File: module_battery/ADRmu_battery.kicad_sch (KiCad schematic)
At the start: 81 parts, among them J101 Harting 09042326831, Q101 Q_NMOS_GDS, Q102 Q_NMOS_GDS, U101 BQ7791500, U102 LTC4079, U103 L7812

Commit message: Update ADRmu_battery.kicad_sch
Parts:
- removed NT101: NetTie_2, NetTie:NetTie-2_SMD_Pad2.0mm, symbol Device:NetTie_2
- added F?: 2A, Fuse:Fuse_1812_4532Metric, symbol Device:Polyfuse
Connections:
- net -BATT: now also F?.1; no longer R107.1, R108.1
- net GND: now also R107.1, R108.1, F?.2

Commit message: asdf
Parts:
- gave numbers to parts that had none: 26
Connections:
- net -BATT: no longer R106.1
- net GND: now also R106.1
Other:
- moved on the sheet: C105

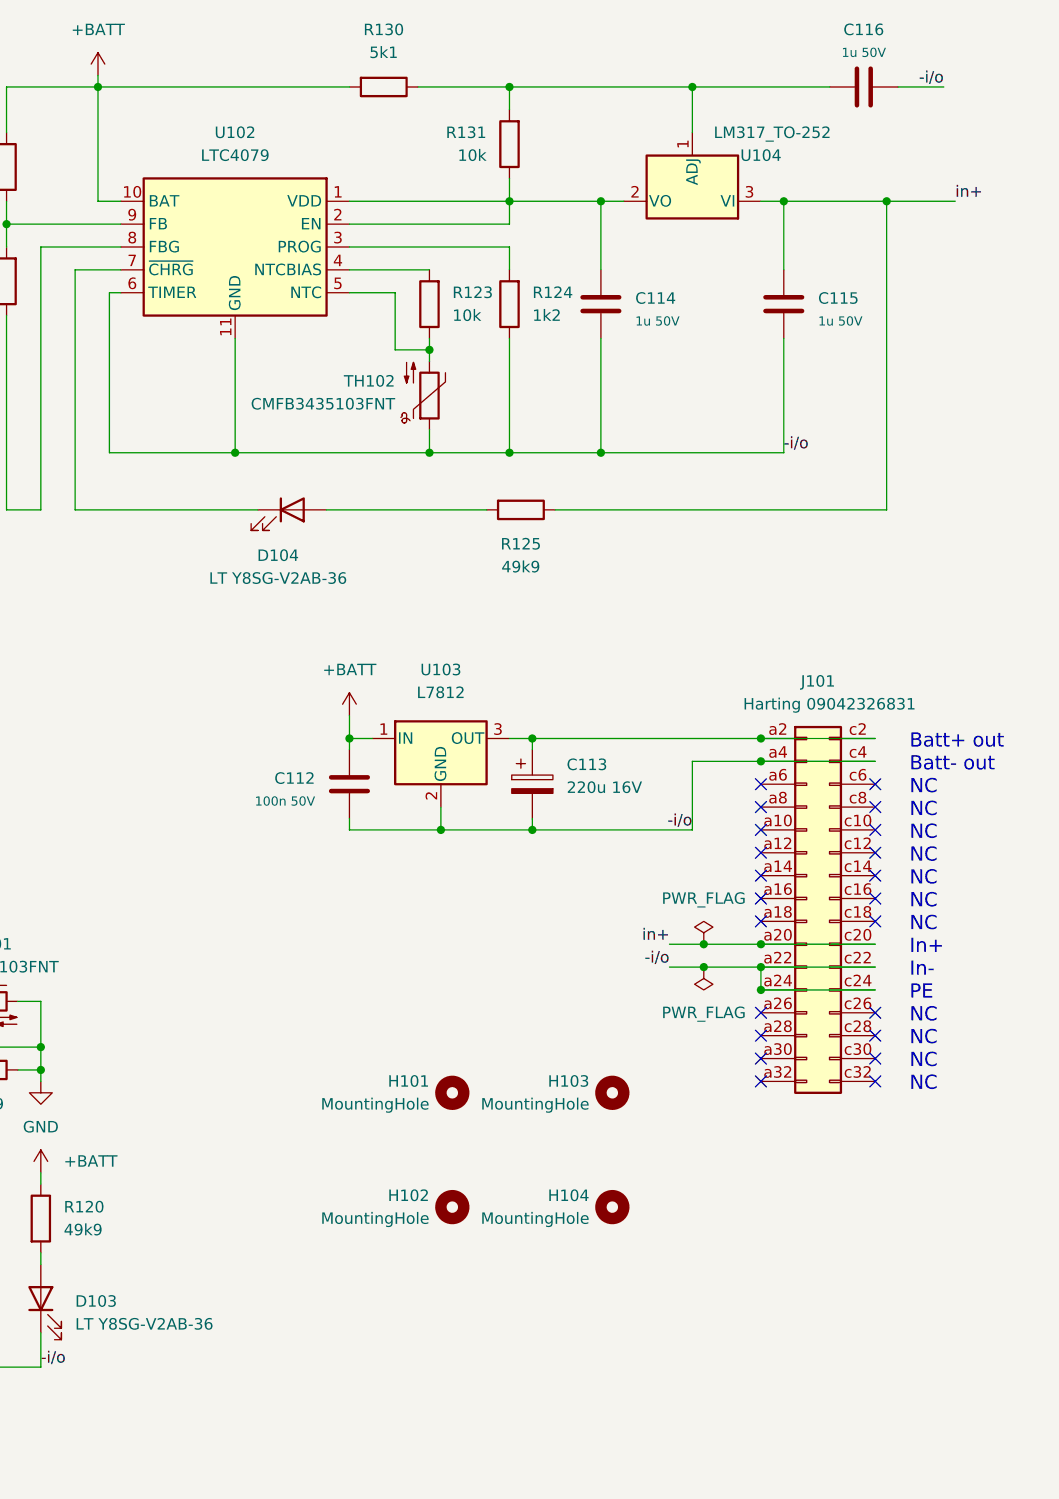
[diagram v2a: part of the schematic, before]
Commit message: battery module rev 0.3 routed
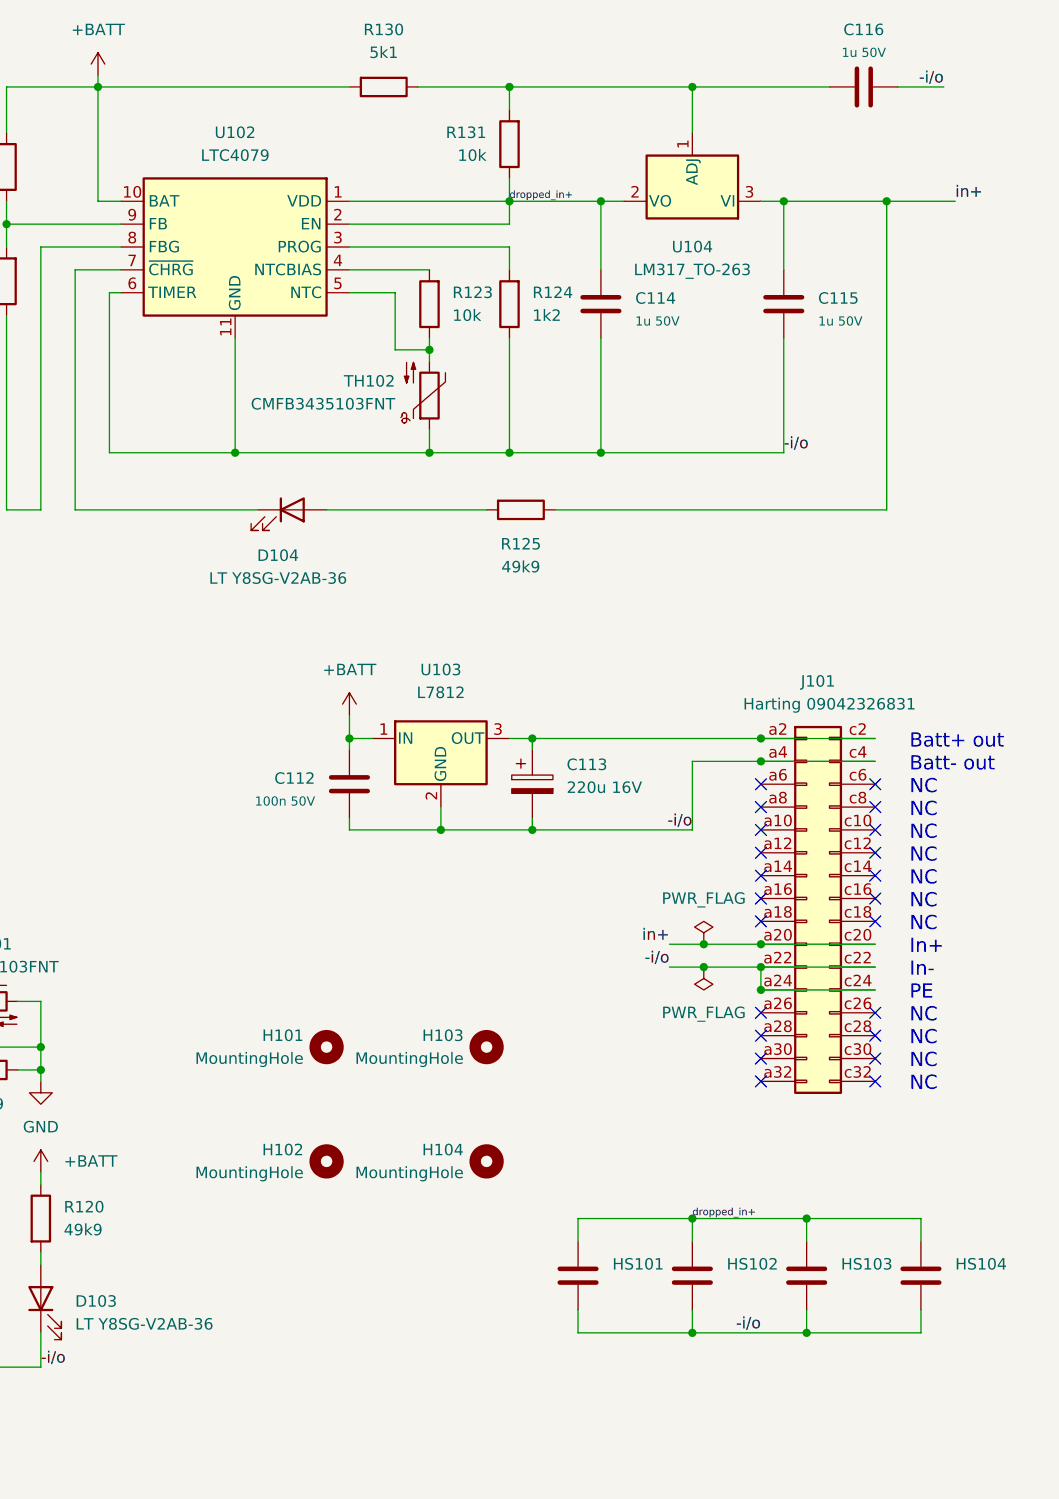
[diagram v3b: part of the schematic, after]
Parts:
- removed U104: LM317_TO-252, Package_TO_SOT_SMD:TO-252-2, symbol Regulator_Linear:LM317_TO-252
- added HS101, HS102, HS103, HS104: THJP1206AST1, Capacitor_SMD:C_1206_3216Metric, symbol Device:C
- added U104: LM317_TO-263, Package_TO_SOT_SMD:TO-263-2, symbol Regulator_Linear:LM317_TO-263
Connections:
- net -i/o: now also HS101.2, HS102.2, HS103.2, HS104.2
- net in+: now also U104.3 (VI)
- net at C116.1, R130.1, R131.2: now also U104.1 (ADJ)
- net dropped_in+: now reaches C114.1, R131.1, U102.1 (VDD), U102.2 (EN)
- net dropped_in+: now also HS101.1, HS102.1, HS103.1, HS104.1, U104.2 (VO)
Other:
- moved on the sheet: H101, H102, H103, H104

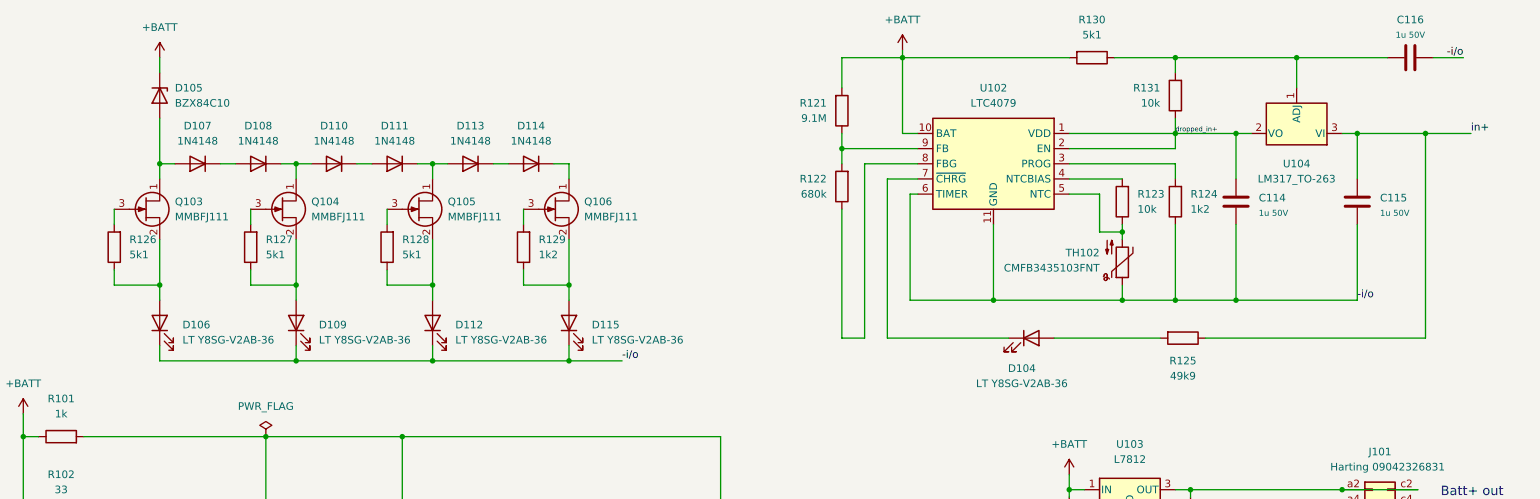
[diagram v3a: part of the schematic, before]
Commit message: minor bug fixes for battery module
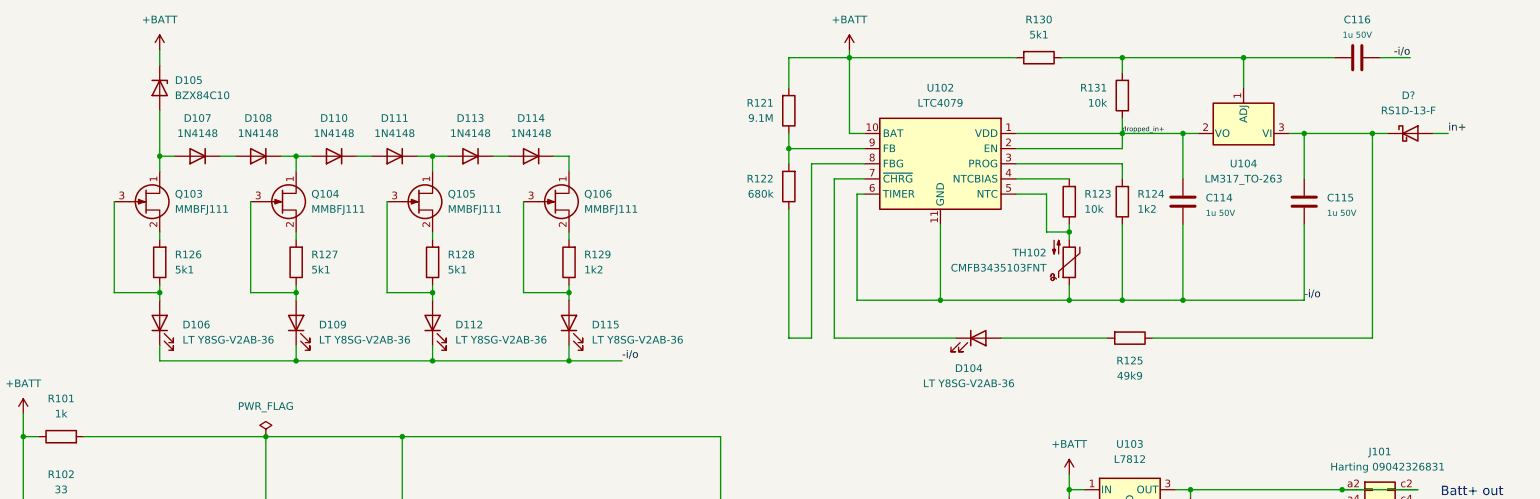
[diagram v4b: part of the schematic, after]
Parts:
- added D?: RS1D-13-F, Diode_SMD:D_SMA, symbol Device:D_Schottky
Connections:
- net in+: now also D?.2 (A); no longer C115.1, R125.1, U104.3 (VI)
- net at D112.2 (A), R128.1: now also Q105.3 (G); no longer Q105.2 (S)
- net at R128.2: now also Q105.2 (S); no longer Q105.3 (G)
- net at D115.2 (A), R129.1: now also Q106.3 (G); no longer Q106.2 (S)
- net at D106.2 (A), R126.1: now also Q103.3 (G); no longer Q103.2 (S)
- net at R126.2: now also Q103.2 (S); no longer Q103.3 (G)
- net at R129.2: now also Q106.2 (S); no longer Q106.3 (G)
- net at D109.2 (A), R127.1: now also Q104.3 (G); no longer Q104.2 (S)
- net at R127.2: now also Q104.2 (S); no longer Q104.3 (G)
- new net: C115.1, D?.1 (K), R125.1, U104.3 (VI)
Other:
- moved on the sheet: C114, C115, C116, D104, D105, D107, D108, D110, D111, D113, D114, Q103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

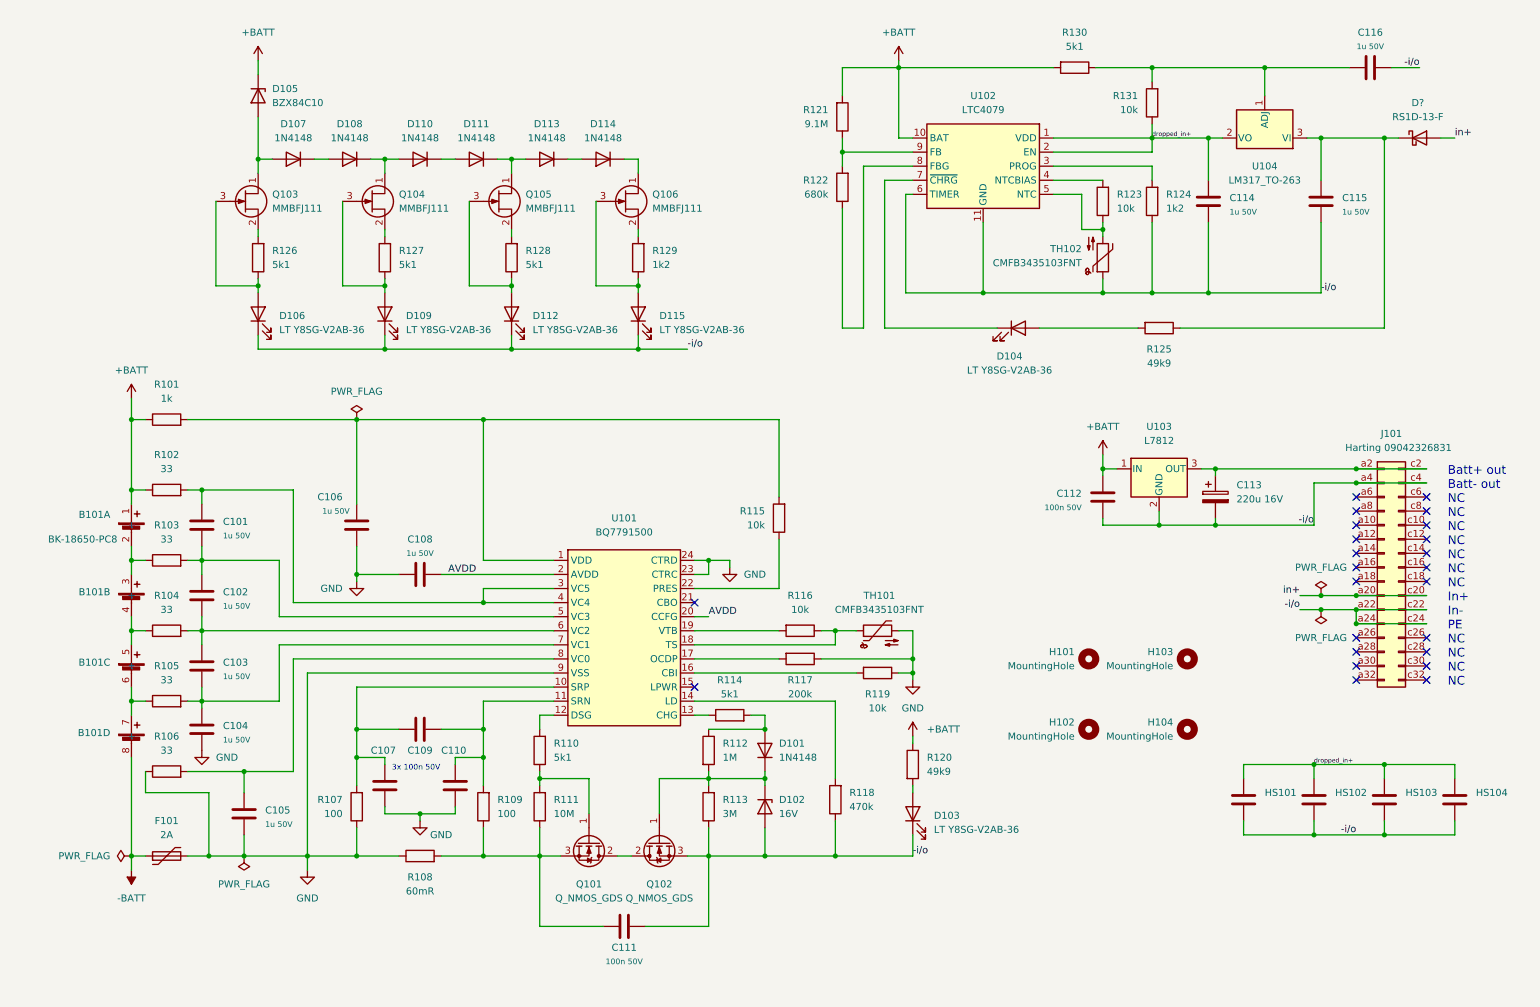
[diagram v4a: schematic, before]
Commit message: Battery module Rev 0.4 routed
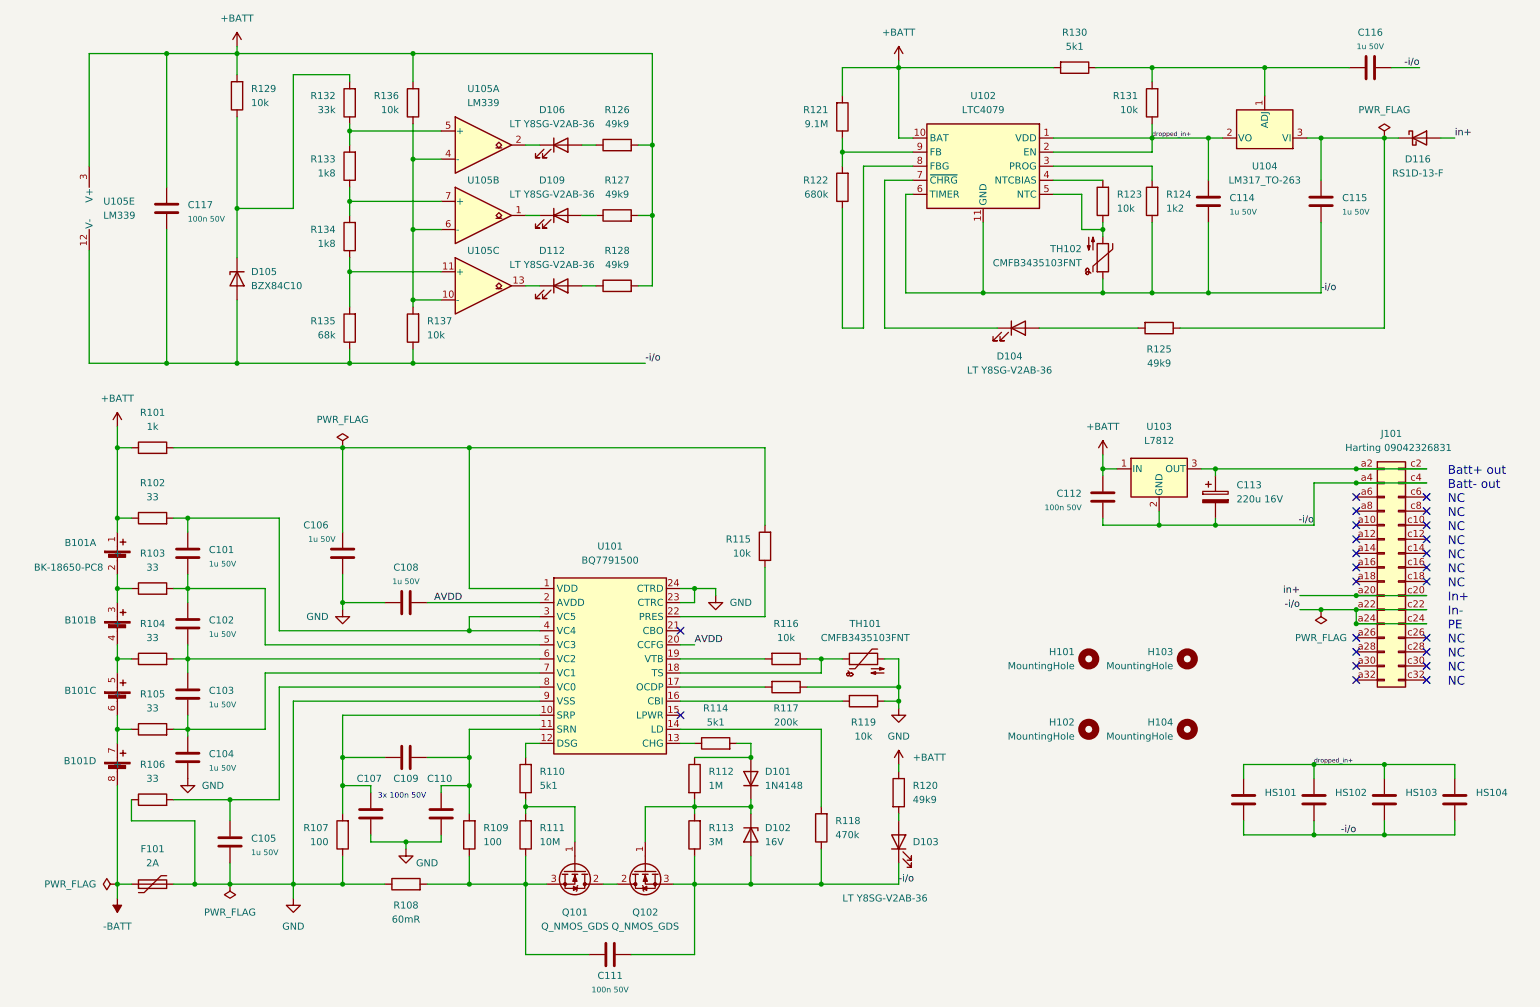
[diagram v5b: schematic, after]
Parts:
- removed D107, D108, D110, D111, D113, D114: 1N4148, Diode_SMD:D_SOD-123, symbol Device:D
- removed D115: LT Y8SG-V2AB-36, LED_SMD:LED_1206_3216Metric, symbol Device:LED
- removed Q103, Q104, Q105, Q106: MMBFJ111, Package_TO_SOT_SMD:SOT-23, symbol Transistor_FET:MMBFJ111
- added C117: 100n 50V, Capacitor_SMD:C_0805_2012Metric, symbol Device:C
- added R132: 33k, Resistor_SMD:R_0805_2012Metric, symbol Device:R
- added R133, R134: 1k8, Resistor_SMD:R_0805_2012Metric, symbol Device:R
- added R135: 68k, Resistor_SMD:R_0805_2012Metric, symbol Device:R
- added R136, R137: 10k, Resistor_SMD:R_0805_2012Metric, symbol Device:R
- added U105: LM339, Package_SO:SOIC-14_3.9x8.7mm_P1.27mm, symbol Comparator:LM339
- R126, R127, R128: value 5k1 -> 49k9
- R129: value 1k2 -> 10k
- gave numbers to parts that had none: 1
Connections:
- net +BATT: now also R126.2, R127.2, R128.2, R129.2, C117.2, R136.2, U105.3 (V+); no longer D105.3 (K)
- net -i/o: now also D105.1 (A), C117.1, R135.1, R137.1, U105.12 (V-); no longer D106.1 (K), D109.1 (K), D112.1 (K)
- net at R129.1: now also D105.3 (K), R132.2
- new net: D106.1 (K), U105.2
- new net: R136.1, R137.2, U105.10 (-), U105.4 (-), U105.6 (-)
- new net: R132.1, R133.2, U105.5 (+)
- new net: R134.1, R135.2, U105.11 (+)
- new net: R133.1, R134.2, U105.7 (+)
- new net: D112.1 (K), U105.13
- new net: D109.1 (K), U105.1
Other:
- moved on the sheet: B101A, B101B, B101C, B101D, C101, C102, C103, C104, C105, C106, C107, C108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

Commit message: Battery module Rev 0.6 update
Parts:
- removed R123: 10k, Resistor_SMD:R_0805_2012Metric, symbol Device:R
- H101, H102, H103, H104: footprint MountingHole:MountingHole_4.3mm_M4 -> MountingHole:MountingHole_5.3mm_M5
- R132: value 33k -> 22k
- R133, R134: value 1k8 -> 6k8
- R135: value 68k -> 82k
- TH102: value CMFB3435103FNT -> Alternative 10k NTC; footprint Resistor_SMD:R_0805_2012Metric -> Resistor_THT:R_Axial_DIN0204_L3.6mm_D1.6mm_P2.54mm_Vertical
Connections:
- net -i/o: now also U102.5 (NTC); no longer TH102.1
- net GND: now also TH102.2
- net at R116.1, TH101.1, U101.18 (TS): now also TH102.1
- no-connect marks 24 -> 25

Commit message: Update ADRmu_battery.kicad_sch
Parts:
- R121: value 9.1M -> 2M
- R122: value 680k -> 150k
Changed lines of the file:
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@@
       (effects (font (size 1.27 1.27)) (justify left))
     )
-    (property "Value" "680k" (id 1) (at 156.21 46.9899 0)
+    (property "Value" "150k" (id 1) (at 156.21 46.9899 0)
       (effects (font (size 1.27 1.27)) (justify left))
     )
@@
       (effects (font (size 1.27 1.27)) (justify right))
     )
-    (property "Value" "9.1M" (id 1) (at 156.21 34.2899 0)
+    (property "Value" "2M" (id 1) (at 156.21 34.2899 0)
       (effects (font (size 1.27 1.27)) (justify right))
     )
@@
     )
     (path "/ebe4d216-6e37-4339-b1fa-650a1a7c8757"
-      (reference "R121") (unit 1) (value "9.1M") (footprint "Resistor_SMD:R_0805_2012Metric")
+      (reference "R121") (unit 1) (value "2M") (footprint "Resistor_SMD:R_0805_2012Metric")
     )
     (path "/85232871-7690-4091-9c3c-7e30ca7a3e94"
-      (reference "R122") (unit 1) (value "680k") (footprint "Resistor_SMD:R_0805_2012Metric")
+      (reference "R122") (unit 1) (value "150k") (footprint "Resistor_SMD:R_0805_2012Metric")
     )
     (path "/e21c3568-b1a1-45b7-8ff2-d3a87b7d6b6c"
